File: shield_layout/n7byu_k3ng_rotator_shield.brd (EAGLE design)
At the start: 53.3 x 59.7 mm, 34 parts, among them J1 EL, J10 ARDisable, J11 ROTCABLE, J2 AZ, J3 ELToggle, J4 ELToggle, J5 I2C-OLD, J6 I2C-NEW, J7 PARK, J8 STOP, J9 RST, Q1 2N3904, Q2 2N3904, Q3 2N3904, Q4 2N3904

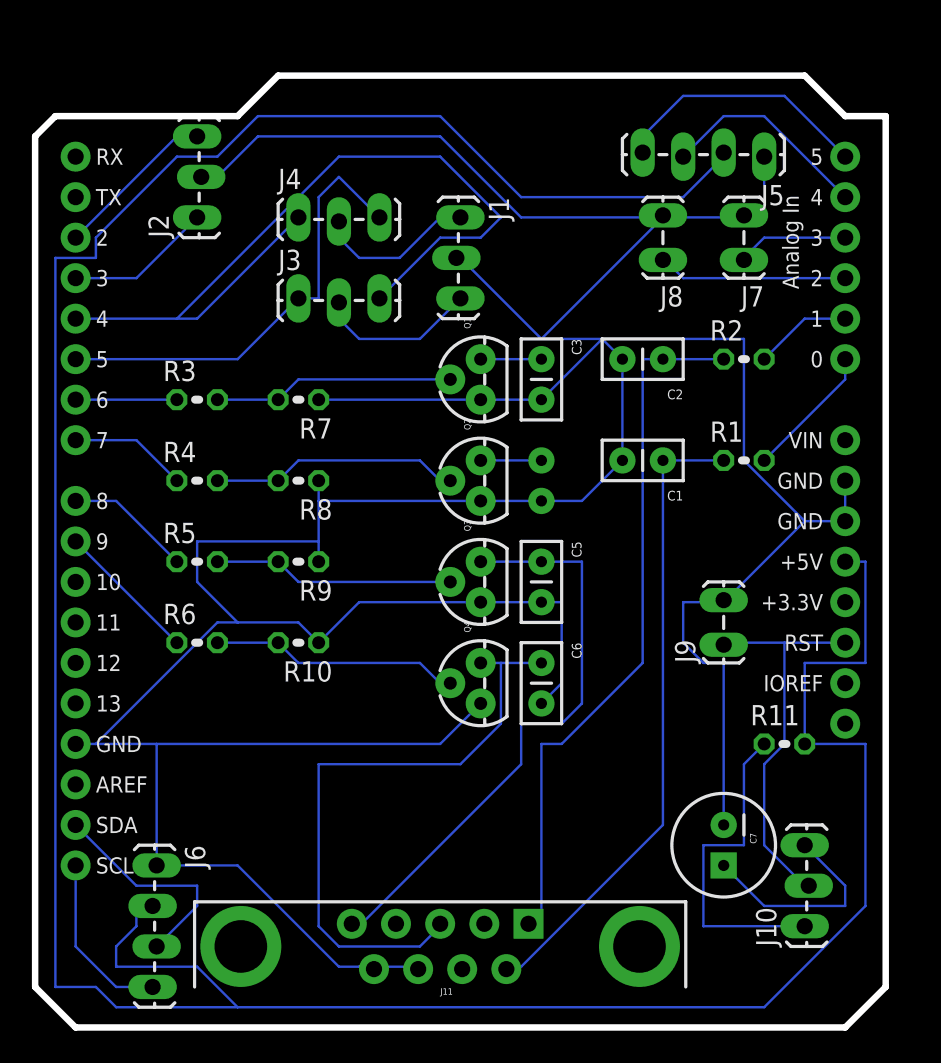
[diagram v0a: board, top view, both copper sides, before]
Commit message: manual re-routing to deal with traces touching pads where they shouldn't.
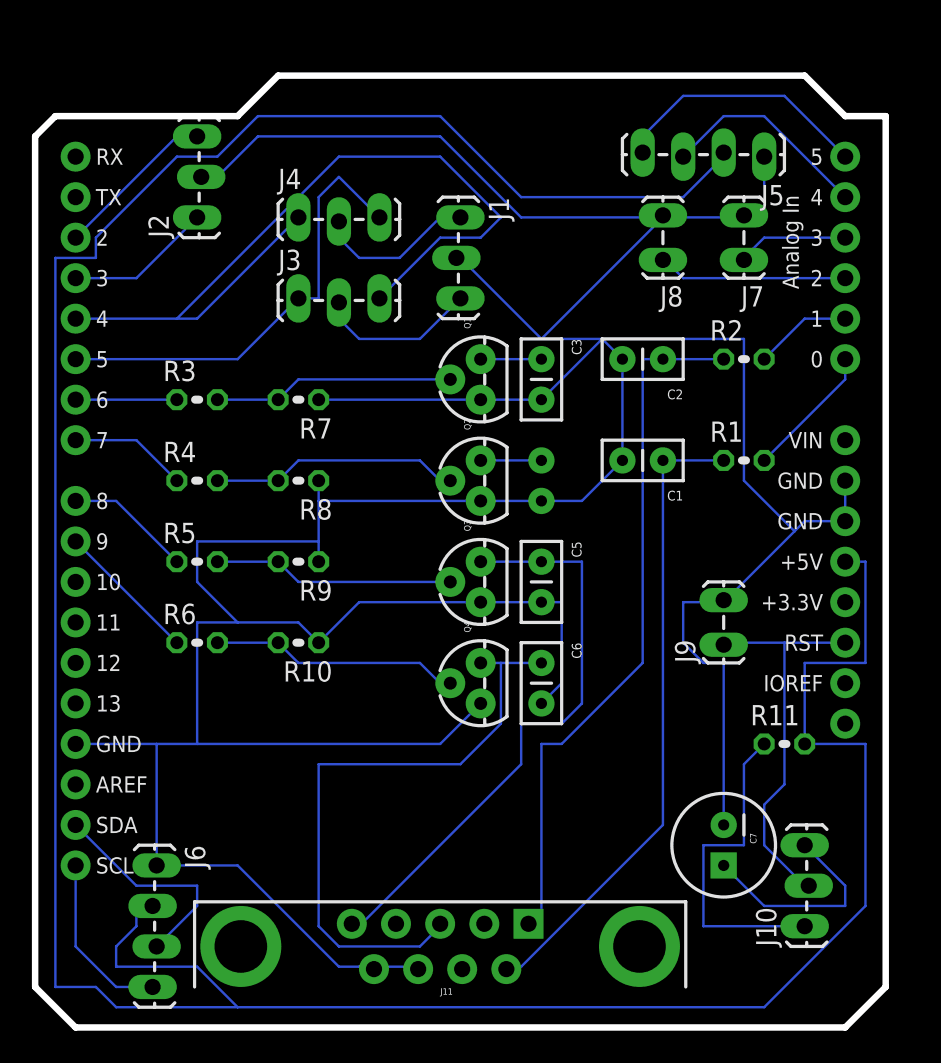
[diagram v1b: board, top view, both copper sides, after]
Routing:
- net GND: track 277.8 -> 276.3 mm
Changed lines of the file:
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@@
 <wire x1="46.99" y1="21.59" x2="46.88" y2="21.44" width="0.1524" layer="16"/>
 <wire x1="30.48" y1="35.56" x2="30.48" y2="27.94" width="0.1524" layer="16"/>
-<wire x1="25.4" y1="35.56" x2="26.67" y2="35.56" width="0.1524" layer="16"/>
-<wire x1="26.67" y1="35.56" x2="30.48" y2="35.56" width="0.1524" layer="16"/>
+<wire x1="25.4" y1="35.56" x2="30.48" y2="35.56" width="0.1524" layer="16"/>
 <wire x1="48.26" y1="35.56" x2="50.8" y2="38.1" width="0.1524" layer="16"/>
-<wire x1="30.48" y1="35.56" x2="48.26" y2="35.56" width="0.1524" layer="16"/>
+<wire x1="30.48" y1="35.56" x2="33.02" y2="35.56" width="0.1524" layer="16"/>
+<wire x1="33.02" y1="35.56" x2="48.26" y2="35.56" width="0.1524" layer="16"/>
 <wire x1="41.91" y1="21.59" x2="43.18" y2="21.59" width="0.1524" layer="16"/>
 <wire x1="35.56" y1="27.94" x2="41.91" y2="21.59" width="0.1524" layer="16"/>
@@
 <wire x1="43.18" y1="21.59" x2="44.11" y2="21.44" width="0.1524" layer="16"/>
 <wire x1="39.37" y1="43.18" x2="40.64" y2="41.91" width="0.1524" layer="16"/>
-<wire x1="34.29" y1="43.18" x2="35.56" y2="43.18" width="0.1524" layer="16"/>
+<wire x1="33.02" y1="43.18" x2="35.56" y2="43.18" width="0.1524" layer="16"/>
 <wire x1="35.56" y1="43.18" x2="39.37" y2="43.18" width="0.1524" layer="16"/>
-<wire x1="26.67" y1="35.56" x2="34.29" y2="43.18" width="0.1524" layer="16"/>
 <wire x1="67.31" y1="68.58" x2="62.23" y2="68.58" width="0.1524" layer="16"/>
 <wire x1="36.83" y1="73.66" x2="34.29" y2="71.12" width="0.1524" layer="16"/>
@@
 <wire x1="67.31" y1="68.58" x2="68.58" y2="68.58" width="0.1524" layer="16"/>
 <wire x1="67.31" y1="68.58" x2="67.31" y2="68.707" width="0.1524" layer="16"/>
-<wire x1="71.12" y1="49.53" x2="66.04" y2="44.45" width="0.1524" layer="16"/>
+<wire x1="71.12" y1="49.53" x2="70.485" y2="48.895" width="0.1524" layer="16"/>
+<wire x1="70.485" y1="48.895" x2="66.04" y2="44.45" width="0.1524" layer="16"/>
 <wire x1="73.66" y1="49.53" x2="71.12" y2="49.53" width="0.1524" layer="16"/>
 <wire x1="66.04" y1="40.64" x2="66.04" y2="30.48" width="0.1524" layer="16"/>
@@
 <wire x1="58.42" y1="60.96" x2="54.61" y2="57.15" width="0.1524" layer="16"/>
 <wire x1="59.69" y1="59.69" x2="59.69" y2="53.34" width="0.1524" layer="16"/>
-<wire x1="67.31" y1="53.34" x2="71.12" y2="49.53" width="0.1524" layer="16"/>
 <wire x1="67.31" y1="60.96" x2="67.31" y2="53.34" width="0.1524" layer="16"/>
 <wire x1="58.42" y1="60.96" x2="67.31" y2="60.96" width="0.1524" layer="16"/>
@@
 <wire x1="33.02" y1="48.26" x2="33.02" y2="45.72" width="0.1524" layer="16"/>
 <wire x1="40.64" y1="48.26" x2="33.02" y2="48.26" width="0.1524" layer="16"/>
+<wire x1="33.02" y1="43.18" x2="33.02" y2="35.56" width="0.1524" layer="16"/>
+<wire x1="67.31" y1="53.34" x2="67.31" y2="52.07" width="0.1524" layer="16"/>
+<wire x1="67.31" y1="52.07" x2="70.485" y2="48.895" width="0.1524" layer="16"/>
 </signal>
 <signal name="N$19">
@@
 <contactref element="J10" pad="2"/>
 <wire x1="68.58" y1="29.21" x2="71.12" y2="26.67" width="0.1524" layer="16"/>
-<wire x1="68.58" y1="34.29" x2="68.58" y2="29.21" width="0.1524" layer="16"/>
-<wire x1="69.85" y1="35.56" x2="68.58" y2="34.29" width="0.1524" layer="16"/>
 <wire x1="69.85" y1="41.91" x2="69.85" y2="35.56" width="0.1524" layer="16"/>
 <wire x1="66.04" y1="41.91" x2="69.85" y2="41.91" width="0.1524" layer="16"/>
@@
 <wire x1="66.04" y1="41.91" x2="66.04" y2="41.783" width="0.1524" layer="16"/>
 <wire x1="69.85" y1="41.91" x2="73.66" y2="41.91" width="0.1524" layer="16"/>
+<wire x1="69.85" y1="35.56" x2="69.85" y2="33.02" width="0.1524" layer="16"/>
+<wire x1="69.85" y1="33.02" x2="68.58" y2="31.75" width="0.1524" layer="16"/>
+<wire x1="68.58" y1="31.75" x2="68.58" y2="29.21" width="0.1524" layer="16"/>
 </signal>
 <signal name="N$21">

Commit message: re-doing with some wider traces and clearences
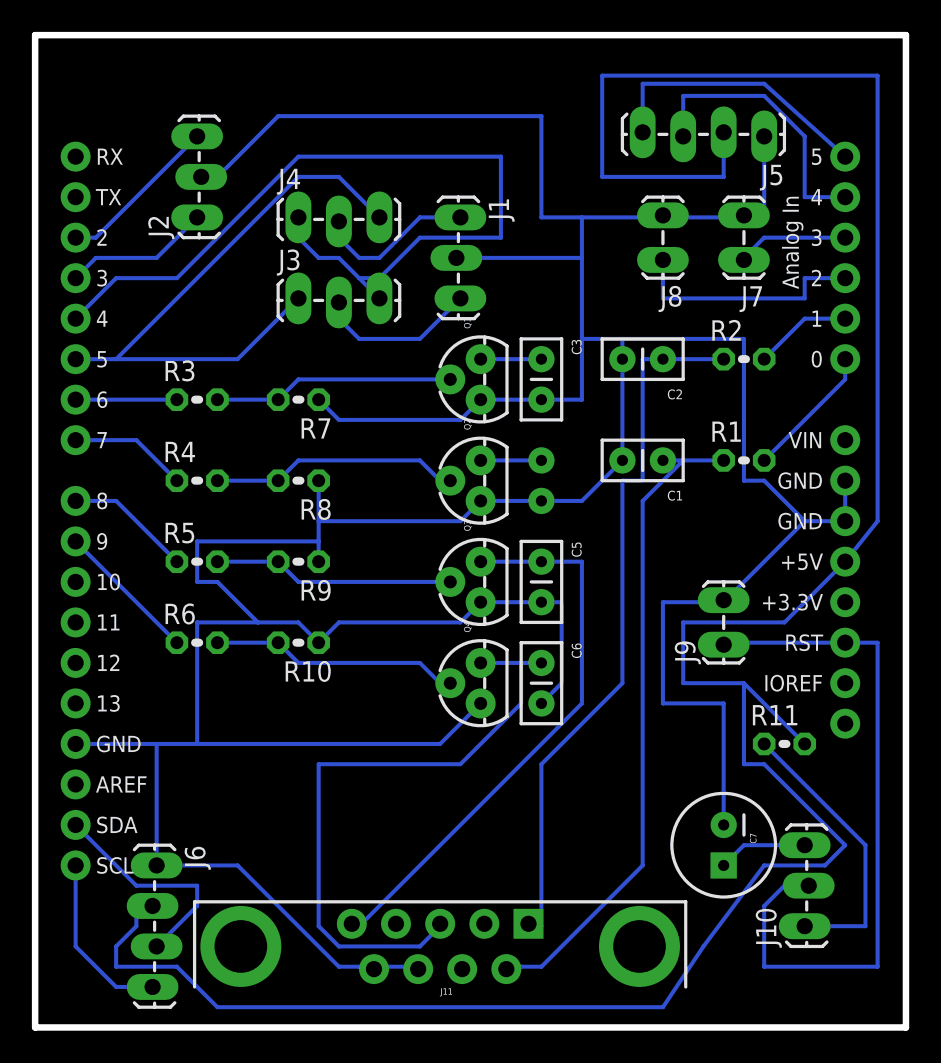
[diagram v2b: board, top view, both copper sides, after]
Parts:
- moved J5 1.27 mm to (68.6, 73.7)
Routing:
- net N$26: track 193.9 -> 160.7 mm
- net N$13: track 24.8 -> 44.3 mm
- net N$24: track 28.6 -> 37.8 mm
- net N$11: track 13.5 -> 5.61 mm
- net GND: track 276.3 -> 284.1 mm
- net N$27: track 13.3 -> 17.6 mm
- net N$22: track 12.1 -> 15.2 mm
- net N$20: track 20.8 -> 17.9 mm
- net N$18: track 37.0 -> 35.5 mm
- net N$23: track 52.4 -> 53.8 mm
- net N$1: track 40.2 -> 41.5 mm
- net N$25: track 16.3 -> 17.5 mm
- net N$12: track 39.1 -> 39.6 mm
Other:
- board size 53.3 x 59.7 mm -> 54.6 x 62.2 mm

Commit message: changed to wider resistor spacing, re-routed traces and re-generated gerbers, etc.
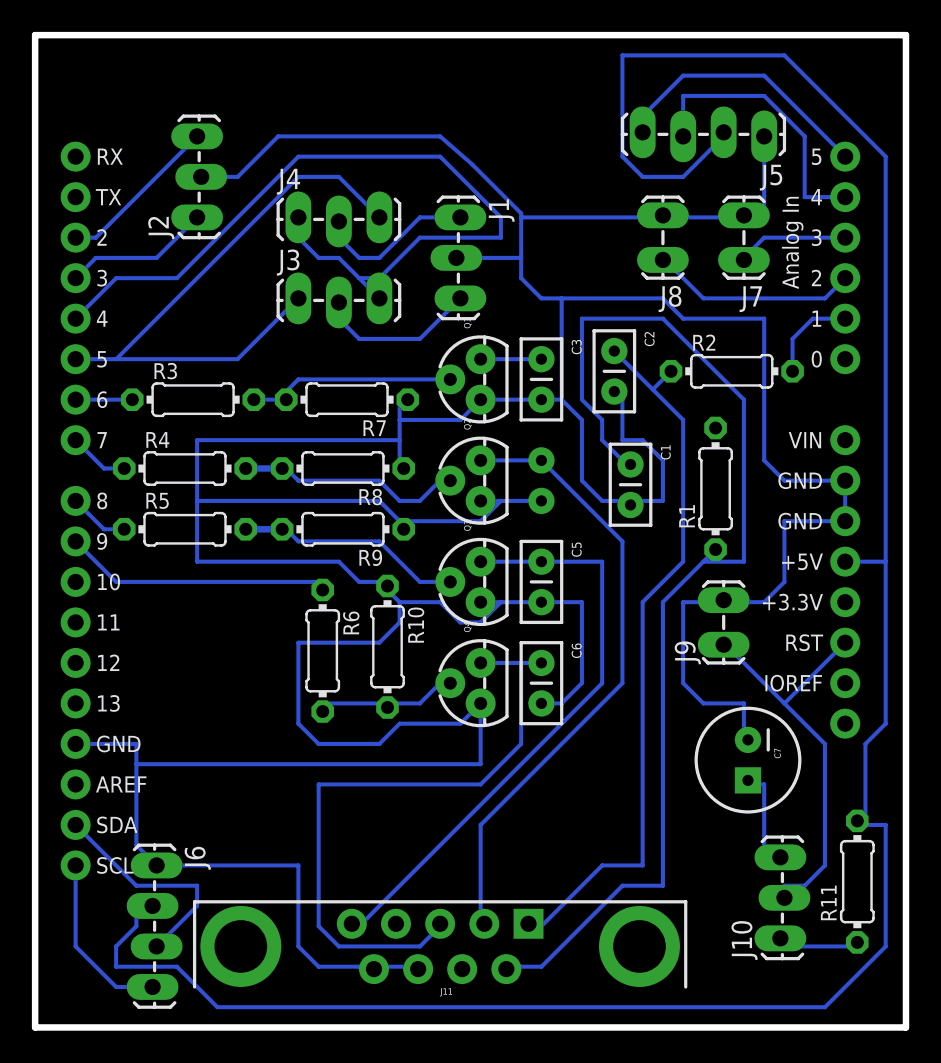
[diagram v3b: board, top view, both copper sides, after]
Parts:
- R1, R10, R11, R2, R3, R4, R5, R6, R7, R8, R9: device resistor:0204V -> resistor:0204/7
- moved R11 9.77 mm to (74.4, 26.9), turned to 90 degrees
- moved R6 7.89 mm to (40.9, 41.4), turned to 270 degrees
- moved R10 5.59 mm to (45.0, 41.7), turned to 270 degrees
- moved C7 5.55 mm to (67.6, 34.5)
- moved R9 3.45 mm to (42.2, 49.0)
- moved C2 3.09 mm to (59.2, 60.2), turned to 270 degrees
- moved R7 3.05 mm to (42.4, 57.1)
- moved R8 2.90 mm to (42.2, 52.8)
- moved R1 2.51 mm to (65.5, 51.6), turned to 90 degrees
- moved R5 2.17 mm to (32.3, 49.0)
- moved C1 2.05 mm to (60.2, 53.1), turned to 270 degrees
- moved J10 1.70 mm to (69.6, 23.4)
- moved R2 1.08 mm to (66.5, 58.9)
- moved R4 1.08 mm to (32.3, 52.8)
- moved R3 0.25 mm to (32.8, 57.1)
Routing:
- net GND: track 284.1 -> 321.1 mm
- net N$10: track 3.81 -> 39.1 mm
- net N$1: track 41.5 -> 69.9 mm
- net N$13: track 44.3 -> 25.9 mm
- net N$26: track 160.7 -> 144.3 mm
- net N$20: track 17.9 -> 6.22 mm
- net N$4: track 8.45 -> 0.00 mm
- net N$19: track 8.98 -> 16.9 mm
- net N$8: track 15.7 -> 9.92 mm
- net N$17: track 7.93 -> 3.78 mm
- net N$16: track 7.40 -> 3.78 mm
- net N$15: track 6.35 -> 3.81 mm
- net N$23: track 53.8 -> 51.6 mm
- net N$22: track 15.2 -> 13.1 mm
- net N$18: track 35.5 -> 37.3 mm
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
